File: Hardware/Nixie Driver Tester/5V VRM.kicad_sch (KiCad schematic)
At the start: 3 parts

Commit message: Using a STM32 instead of a PIC
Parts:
- U3: value ~ -> (none)

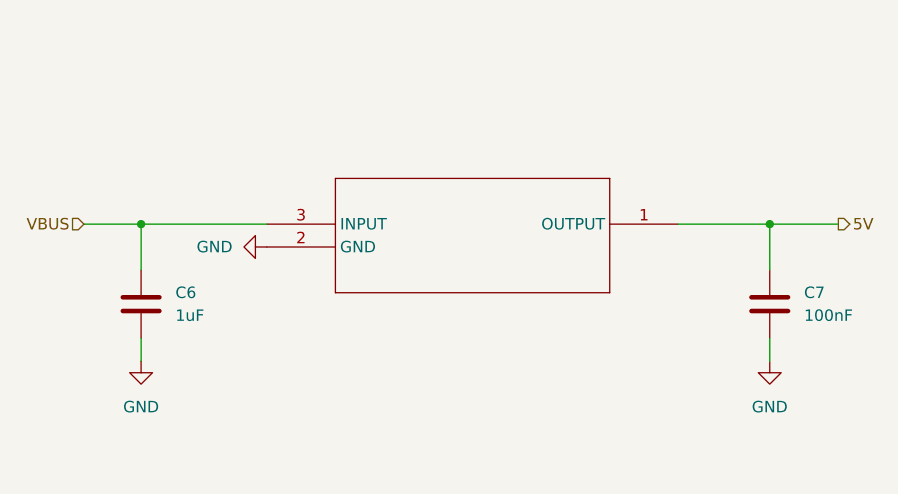
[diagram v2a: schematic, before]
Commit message: Switch mode 3.3V and SMD inductor
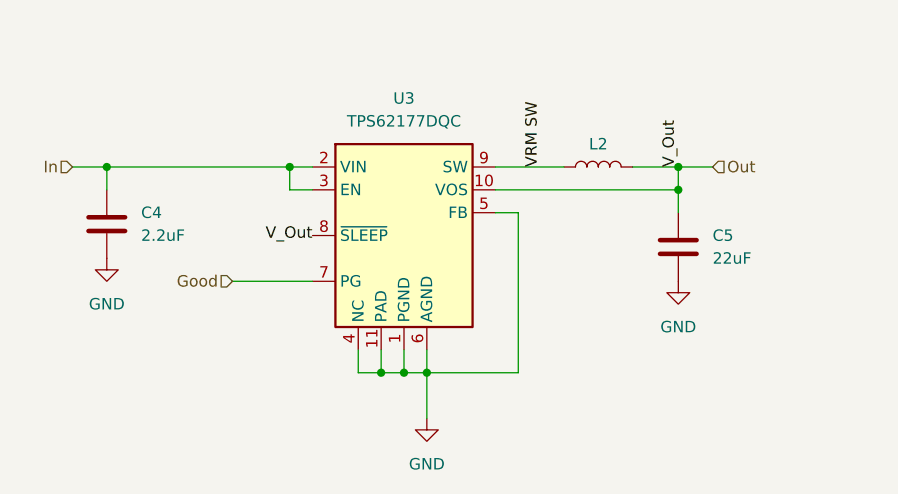
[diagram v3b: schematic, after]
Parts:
- removed C6: 1uF, Capacitor_SMD:C_0805_2012Metric, symbol Device:C
- removed C7: 100nF, Capacitor_SMD:C_0603_1608Metric, symbol Device:C
- removed U3: (no value), Package_TO_SOT_SMD:SOT-89-3, symbol VRM_:AS78L05RTR-E1
- added C4: 2.2uF, Capacitor_SMD:C_0805_2012Metric, symbol Device:C
- added C5: 22uF, Capacitor_SMD:C_0805_2012Metric, symbol Device:C
- added L2: VLS4012CX-100M-1, Inductor_:TDK LPS40xx, symbol Device:L
- added U3: TPS62177DQC, Package_SON:WSON-10-1EP_2x3mm_P0.5mm_EP0.84x2.4mm_ThermalVias, symbol Regulator_Switching:TPS62177DQC
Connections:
- net GND: now also C4.2, C5.2, U3.1 (PGND), U3.11 (PAD), U3.4 (NC), U3.5 (FB), U3.6 (AGND)
- new net Good: U3.7 (PG)
- new net In: C4.1, U3.2 (VIN), U3.3 (EN)
- new net Out: C5.1, L2.2, U3.10 (VOS), U3.8 (~{SLEEP})
- new net VRM SW: L2.1, U3.9 (SW)

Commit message: Added test points
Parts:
- added TP9: 3.3V, TestPoint:TestPoint_Keystone_5015_Micro_Mini, symbol Connector:TestPoint
- renumbered C4 to C5, C5 to C6
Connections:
- net Out: now also TP9.1
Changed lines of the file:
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@@
+	(wire
+		(pts
+			(xy 167.64 76.2) (xy 167.64 86.36)
+		)
+		(stroke
+			(width 0)
+			(type default)
+		)
+	)
 	(wire
 		(pts
@@
 		(dnp no)
 		(fields_autoplaced yes)
-		(property "Reference" "C4"
+		(property "Reference" "C5"
 			(at 107.95 91.4399 0)
 			(show_name no)
@@
 			(project "Nixie Driver Tester"
 				(path "/c2082ee6-4c2e-4b3c-b2d7-410eae192cfe/f02fb26c-0046-487f-b7d5-0718c4f74977"
-					(reference "C4")
+					(reference "C5")
 					(unit 1)
 				)
@@
 		(dnp no)
 		(fields_autoplaced yes)
-		(property "Reference" "#PWR022"
+		(property "Reference" "#PWR024"
 			(at 139.7 120.65 0)
 			(hide yes)
@@
 			(project "Nixie Driver Tester"
 				(path "/c2082ee6-4c2e-4b3c-b2d7-410eae192cfe/f02fb26c-0046-487f-b7d5-0718c4f74977"
-					(reference "#PWR022")
+					(reference "#PWR024")
 					(unit 1)
 				)
@@
 		(dnp no)
 		(fields_autoplaced yes)
-		(property "Reference" "C5"
+		(property "Reference" "C6"
 			(at 171.45 93.9799 0)
 			(show_name no)
@@
 			(project "Nixie Driver Tester"
 				(path "/c2082ee6-4c2e-4b3c-b2d7-410eae192cfe/f02fb26c-0046-487f-b7d5-0718c4f74977"
-					(reference "C5")
+					(reference "C6")
+					(unit 1)
+				)
+			)
+		)
+	)
+	(symbol
+		(lib_id "Connector:TestPoint")
+		(at 167.64 76.2 0)
+		(unit 1)
+		(body_style 1)
+		(exclude_from_sim no)
+		(in_bom yes)
+		(on_board yes)
+		(in_pos_files yes)
+		(dnp no)
+		(property "Reference" "TP9"
+			(at 165.1 71.12 0)
+			(show_name no)
+			(do_not_autoplace no)
+			(effects
+				(font
+					(size 1.27 1.27)
+				)
+				(justify left)
+			)
+		)
+		(property "Value" "3.3V"
+			(at 170.18 74.1679 0)
+			(hide yes)
+			(show_name no)
+			(do_not_autoplace no)
+			(effects
+				(font
+					(size 1.27 1.27)
+				)
+				(justify left)
+			)
+		)
+		(property "Footprint" "TestPoint:TestPoint_Keystone_5015_Micro_Mini"
+			(at 172.72 76.2 0)
+			(hide yes)
+			(show_name no)
+			(do_not_autoplace no)
+			(effects
+				(font
+					(size 1.27 1.27)
+				)
+			)
+		)
+		(property "Datasheet" ""
+			(at 172.72 76.2 0)
+			(hide yes)
+			(show_name no)
+			(do_not_autoplace no)
+			(effects
+				(font
+					(size 1.27 1.27)
+				)
+			)
+		)
+		(property "Description" "test point"
+			(at 167.64 76.2 0)
+			(hide yes)
+			(show_name no)
+			(do_not_autoplace no)
+			(effects
+				(font
+					(size 1.27 1.27)
+				)
+			)
+		)
+		(pin "1"
+		)
+		(instances
+			(project "Nixie Driver Tester"
+				(path "/c2082ee6-4c2e-4b3c-b2d7-410eae192cfe/f02fb26c-0046-487f-b7d5-0718c4f74977"
+					(reference "TP9")
 					(unit 1)
 				)
@@
 		(dnp no)
 		(fields_autoplaced yes)
-		(property "Reference" "#PWR021"
+		(property "Reference" "#PWR023"
 			(at 104.14 102.87 0)
 			(hide yes)
@@
 			(project "Nixie Driver Tester"
 				(path "/c2082ee6-4c2e-4b3c-b2d7-410eae192cfe/f02fb26c-0046-487f-b7d5-0718c4f74977"
-					(reference "#PWR021")
+					(reference "#PWR023")
 					(unit 1)
 				)
@@
 		(dnp no)
 		(fields_autoplaced yes)
-		(property "Reference" "#PWR023"
+		(property "Reference" "#PWR025"
 			(at 167.64 105.41 0)
 			(hide yes)
@@
 			(project "Nixie Driver Tester"
 				(path "/c2082ee6-4c2e-4b3c-b2d7-410eae192cfe/f02fb26c-0046-487f-b7d5-0718c4f74977"
-					(reference "#PWR023")
+					(reference "#PWR025")
 					(unit 1)
 				)
